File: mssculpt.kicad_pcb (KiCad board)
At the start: 2 copper layers, 47.5 x 40 mm, 9 parts, among them J1 keyboard, J2 debug, J3 power, U1 E73-2G4M04S-52832

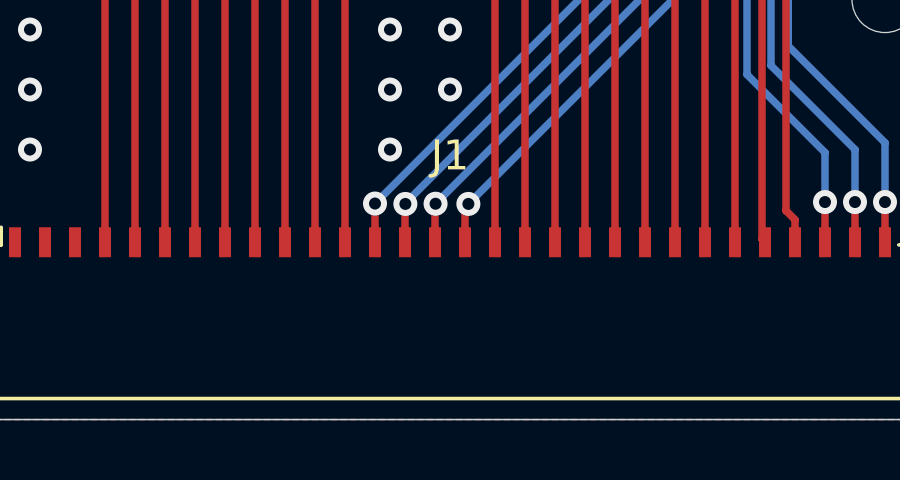
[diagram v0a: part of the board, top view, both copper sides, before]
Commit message: add jlcpcb order number location
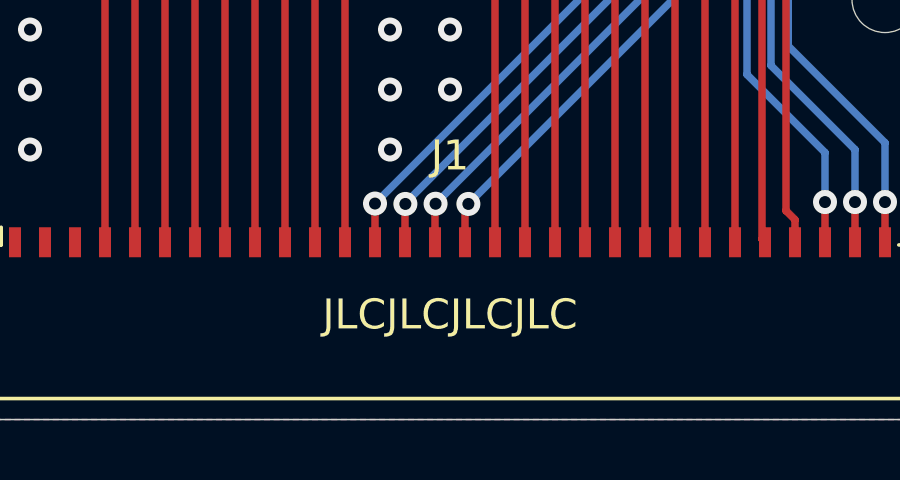
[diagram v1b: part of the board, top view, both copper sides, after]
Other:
- board text added: "JLCJLCJLCJLC"
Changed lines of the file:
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@@
   (general
     (thickness 1.6)
-    (drawings 18)
+    (drawings 19)
     (tracks 286)
     (zones 0)
@@
     )
   )
+  (gr_text JLCJLCJLCJLC (at 174 116.5) (layer F.SilkS)
+    (effects (font (size 1 1) (thickness 0.15)))
+  )
   (gr_text v1.0 (at 172.91 104.05) (layer F.SilkS)

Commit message: backup
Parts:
- removed J3: power, mssculpt:JST_ZH_1x02_P1.50mm_Vertical
- removed U1: E73-2G4M04S-52832, RF_Module:E73-2G4M04S
